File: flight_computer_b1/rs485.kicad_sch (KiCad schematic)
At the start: 1 part, among them U7 MIC94161YCS-TR

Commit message: flight computer updates
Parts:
- removed U7: MIC94161YCS-TR, avi_lib:MIC94161YCS_TR, symbol avi_lib:MIC94161YCS-TR
- added CR5: ST490ABDR, SO-8_STM, symbol avi_lib:ST490ABDR
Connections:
- net 5V: now also CR5.1 (VCC)
- net GND: now also CR5.4 (GND)
- new net RS485_RX+: CR5.8 (A)
- new net RS485_RX-: CR5.7 (B)
- new net RS485_TX+: CR5.5 (Y)
- new net RS485_TX-: CR5.6 (Z)
- new net UART_RX: CR5.2 (R)
- new net UART_TX: CR5.3 (D)
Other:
- note removed: "ideal diode controller"
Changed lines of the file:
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@@
 	(generator_version "9.0")
 	(paper "A4")
-	(text "ideal diode controller"
-		(exclude_from_sim no)
-		(at 134.62 102.87 0)
-		(effects
-			(font
-				(size 1.27 1.27)
-			)
-		)
-	)
-	(junction
-		(at 106.68 92.71)
-		(diameter 0)
-		(color 0 0 0 0)
-	)
-	(junction
-		(at 162.56 95.25)
-		(diameter 0)
-		(color 0 0 0 0)
-	)
-	(wire
-		(pts
-			(xy 162.56 92.71) (xy 162.56 95.25)
-		)
-		(stroke
-			(width 0)
-			(type default)
-		)
-	)
-	(wire
-		(pts
-			(xy 106.68 92.71) (xy 106.68 95.25)
-		)
-		(stroke
-			(width 0)
-			(type default)
-		)
-	)
-	(wire
-		(pts
-			(xy 162.56 95.25) (xy 165.1 95.25)
-		)
-		(stroke
-			(width 0)
-			(type default)
-		)
-	)
-	(wire
-		(pts
-			(xy 106.68 90.17) (xy 106.68 92.71)
-		)
-		(stroke
-			(width 0)
-			(type default)
-		)
-	)
-	(wire
-		(pts
-			(xy 100.33 92.71) (xy 106.68 92.71)
-		)
-		(stroke
-			(width 0)
-			(type default)
-		)
-	)
-	(wire
-		(pts
-			(xy 163.83 90.17) (xy 162.56 90.17)
-		)
-		(stroke
-			(width 0)
-			(type default)
+	(hierarchical_label "UART_TX"
+		(shape input)
+		(at 137.16 96.52 180)
+		(effects
+			(font
+				(size 1.27 1.27)
+			)
+			(justify right)
+		)
+	)
+	(hierarchical_label "UART_RX"
+		(shape input)
+		(at 137.16 93.98 180)
+		(effects
+			(font
+				(size 1.27 1.27)
+			)
+			(justify right)
+		)
+	)
+	(hierarchical_label "RS485_TX+"
+		(shape input)
+		(at 177.8 99.06 0)
+		(effects
+			(font
+				(size 1.27 1.27)
+			)
+			(justify left)
+		)
+	)
+	(hierarchical_label "RS485_TX-"
+		(shape input)
+		(at 177.8 96.52 0)
+		(effects
+			(font
+				(size 1.27 1.27)
+			)
+			(justify left)
+		)
+	)
+	(hierarchical_label "RS485_RX+"
+		(shape input)
+		(at 177.8 91.44 0)
+		(effects
+			(font
+				(size 1.27 1.27)
+			)
+			(justify left)
+		)
+	)
+	(hierarchical_label "RS485_RX-"
+		(shape input)
+		(at 177.8 93.98 0)
+		(effects
+			(font
+				(size 1.27 1.27)
+			)
+			(justify left)
 		)
 	)
 	(hierarchical_label "5V"
 		(shape input)
-		(at 100.33 92.71 180)
+		(at 137.16 91.44 180)
 		(effects
 			(font
@@
 			)
 			(justify right)
-		)
-	)
-	(hierarchical_label "5V_ISO"
-		(shape input)
-		(at 165.1 95.25 0)
-		(effects
-			(font
-				(size 1.27 1.27)
-			)
-			(justify left)
 		)
 	)
 	(symbol
 		(lib_id "power:GND")
-		(at 163.83 90.17 90)
+		(at 137.16 99.06 0)
 		(unit 1)
 		(exclude_from_sim no)
@@
 		(dnp no)
 		(fields_autoplaced yes)
-		(property "Reference" "#PWR055"
-			(at 170.18 90.17 0)
+		(property "Reference" "#PWR056"
+			(at 137.16 105.41 0)
 			(effects
 				(font
@@
 		)
 		(property "Value" "GND"
-			(at 167.64 90.1699 90)
-			(effects
-				(font
-					(size 1.27 1.27)
-				)
-				(justify right)
+			(at 137.16 104.14 0)
+			(effects
+				(font
+					(size 1.27 1.27)
+				)
 			)
 		)
 		(property "Footprint" ""
-			(at 163.83 90.17 0)
+			(at 137.16 99.06 0)
 			(effects
 				(font
@@
 		)
 		(property "Datasheet" ""
-			(at 163.83 90.17 0)
+			(at 137.16 99.06 0)
 			(effects
 				(font
@@
 		)
 		(property "Description" "Power symbol creates a global label with name \"GND\" , ground"
-			(at 163.83 90.17 0)
+			(at 137.16 99.06 0)
 			(effects
 				(font
@@
 		)
 		(instances
-			(project "flight_computer"
-				(path "/b71a7b79-cdb5-4e38-a72c-0daaa3474f05/4c75cebc-ee68-4292-a47b-c723457cf341"
-					(reference "#PWR055")
+			(project ""
+				(path "/b71a7b79-cdb5-4e38-a72c-0daaa3474f05/7fe62967-9424-47cf-ae6f-da5e7ca252e6"
+					(reference "#PWR056")
 					(unit 1)
 				)
@@
 	)
 	(symbol
-		(lib_id "avi_lib:MIC94161YCS-TR")
-		(at 106.68 90.17 0)
+		(lib_id "avi_lib:ST490ABDR")
+		(at 137.16 91.44 0)
 		(unit 1)
 		(exclude_from_sim no)
@@
 		(dnp no)
 		(fields_autoplaced yes)
-		(property "Reference" "U7"
-			(at 134.62 80.01 0)
+		(property "Reference" "CR5"
+			(at 157.48 81.28 0)
 			(effects
 				(font
@@
 			)
 		)
-		(property "Value" "MIC94161YCS-TR"
-			(at 134.62 82.55 0)
+		(property "Value" "ST490ABDR"
+			(at 157.48 83.82 0)
 			(effects
 				(font
@@
 			)
 		)
-		(property "Footprint" "avi_lib:MIC94161YCS_TR"
-			(at 106.68 90.17 0)
+		(property "Footprint" "SO-8_STM"
+			(at 137.16 91.44 0)
 			(effects
 				(font
@@
 			)
 		)
-		(property "Datasheet" "MIC94161YCS-TR"
-			(at 106.68 90.17 0)
+		(property "Datasheet" "https://www.st.com/resource/en/datasheet/st490ab.pdf"
+			(at 137.16 91.44 0)
 			(effects
 				(font
@@
 		)
 		(property "Description" ""
-			(at 106.68 90.17 0)
-			(effects
-				(font
-					(size 1.27 1.27)
-				)
-				(hide yes)
-			)
-		)
-		(pin "C1"
-		)
-		(pin "B2"
-		)
-		(pin "C2"
-		)
-		(pin "A1"
-		)
-		(pin "B1"
-		)
-		(pin "A2"
+			(at 137.16 91.44 0)
+			(effects
+				(font
+					(size 1.27 1.27)
+				)
+				(hide yes)
+			)
+		)
+		(pin "8"
+		)
+		(pin "1"
+		)
+		(pin "2"
+		)
+		(pin "4"
+		)
+		(pin "7"
+		)
+		(pin "3"
+		)
+		(pin "6"
+		)
+		(pin "5"
 		)
 		(instances
-			(project "flight_computer"
-				(path "/b71a7b79-cdb5-4e38-a72c-0daaa3474f05/4c75cebc-ee68-4292-a47b-c723457cf341"
-					(reference "U7")
+			(project ""
+				(path "/b71a7b79-cdb5-4e38-a72c-0daaa3474f05/7fe62967-9424-47cf-ae6f-da5e7ca252e6"
+					(reference "CR5")
 					(unit 1)
 				)

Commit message: flight computer: added mux and voltage sense channels
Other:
- company: (none) -> Purdue Space Program Liquids
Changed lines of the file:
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@@
 	(generator_version "9.0")
 	(paper "A4")
+	(title_block
+		(date "2025-11-05")
+		(rev "1")
+		(company "Purdue Space Program Liquids")
+	)
 	(hierarchical_label "UART_TX"
 		(shape input)

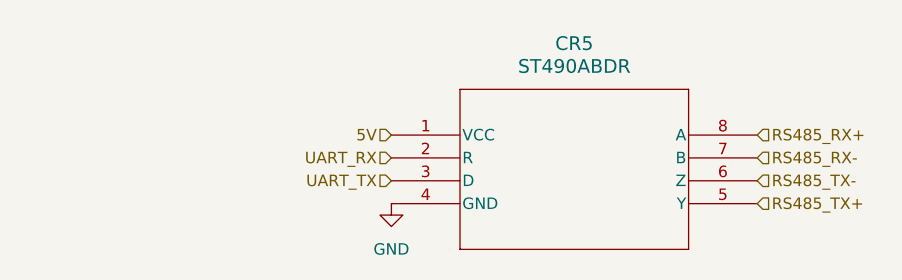
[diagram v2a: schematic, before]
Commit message: flight computer: added pyro circuit and digikey part numbers
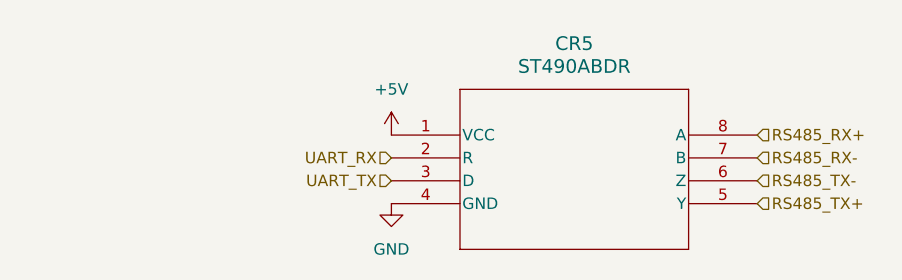
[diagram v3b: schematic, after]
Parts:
- CR5: DIGIKEY PART N (none) -> 497-2091-1-ND
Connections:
- net 5V renamed +5V
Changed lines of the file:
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@@
-		)
-	)
-	(hierarchical_label "5V"
-		(shape input)
-		(at 137.16 91.44 180)
-		(effects
-			(font
-				(size 1.27 1.27)
-			)
-			(justify right)
 		)
 	)
@@
 			)
 		)
+		(property "DIGIKEY PART N" "497-2091-1-ND"
+			(at 137.16 91.44 0)
+			(effects
+				(font
+					(size 1.27 1.27)
+				)
+				(hide yes)
+			)
+		)
 		(pin "8"
 		)
@@
 					(unit 1)
 				)
+			)
+		)
+	)
+	(symbol
+		(lib_id "power:+5V")
+		(at 137.16 91.44 0)
+		(unit 1)
+		(exclude_from_sim no)
+		(in_bom yes)
+		(on_board yes)
+		(dnp no)
+		(fields_autoplaced yes)
+		(property "Reference" "#PWR073"
+			(at 137.16 95.25 0)
+			(effects
+				(font
+					(size 1.27 1.27)
+				)
+				(hide yes)
+			)
+		)
+		(property "Value" "+5V"
+			(at 137.16 86.36 0)
+			(effects
+				(font
+					(size 1.27 1.27)
+				)
+			)
+		)
+		(property "Footprint" ""
+			(at 137.16 91.44 0)
+			(effects
+				(font
+					(size 1.27 1.27)
+				)
+				(hide yes)
+			)
+		)
+		(property "Datasheet" ""
+			(at 137.16 91.44 0)
+			(effects
+				(font
+					(size 1.27 1.27)
+				)
+				(hide yes)
+			)
+		)
+		(property "Description" "Power symbol creates a global label with name \"+5V\""
+			(at 137.16 91.44 0)
+			(effects
+				(font
+					(size 1.27 1.27)
+				)
+				(hide yes)
+			)
+		)
+		(pin "1"
+		)
+		(instances
+			(project ""
+				(path "/b71a7b79-cdb5-4e38-a72c-0daaa3474f05/7fe62967-9424-47cf-ae6f-da5e7ca252e6"
+					(reference "#PWR073")
+					(unit 1)
+				)

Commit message: assigned footprints to capacitors
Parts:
- CR5: footprint SO-8_STM -> avi_footprint:SO-8_STM
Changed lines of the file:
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@@
 			)
 		)
-		(property "Footprint" "SO-8_STM"
+		(property "Footprint" "avi_footprint:SO-8_STM"
 			(at 137.16 91.44 0)
 			(effects
